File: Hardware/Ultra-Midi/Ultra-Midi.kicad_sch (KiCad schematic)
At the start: 28 parts, among them J1 Conn_01x02, J14 CUI_SD-50BV, J16 CUI_SD-50BV, J17 CUI_SD-50BV, J2 Conn_01x02, J3 Conn_01x02, J4 Conn_01x06, U1 ADuM226, U2 AP7370

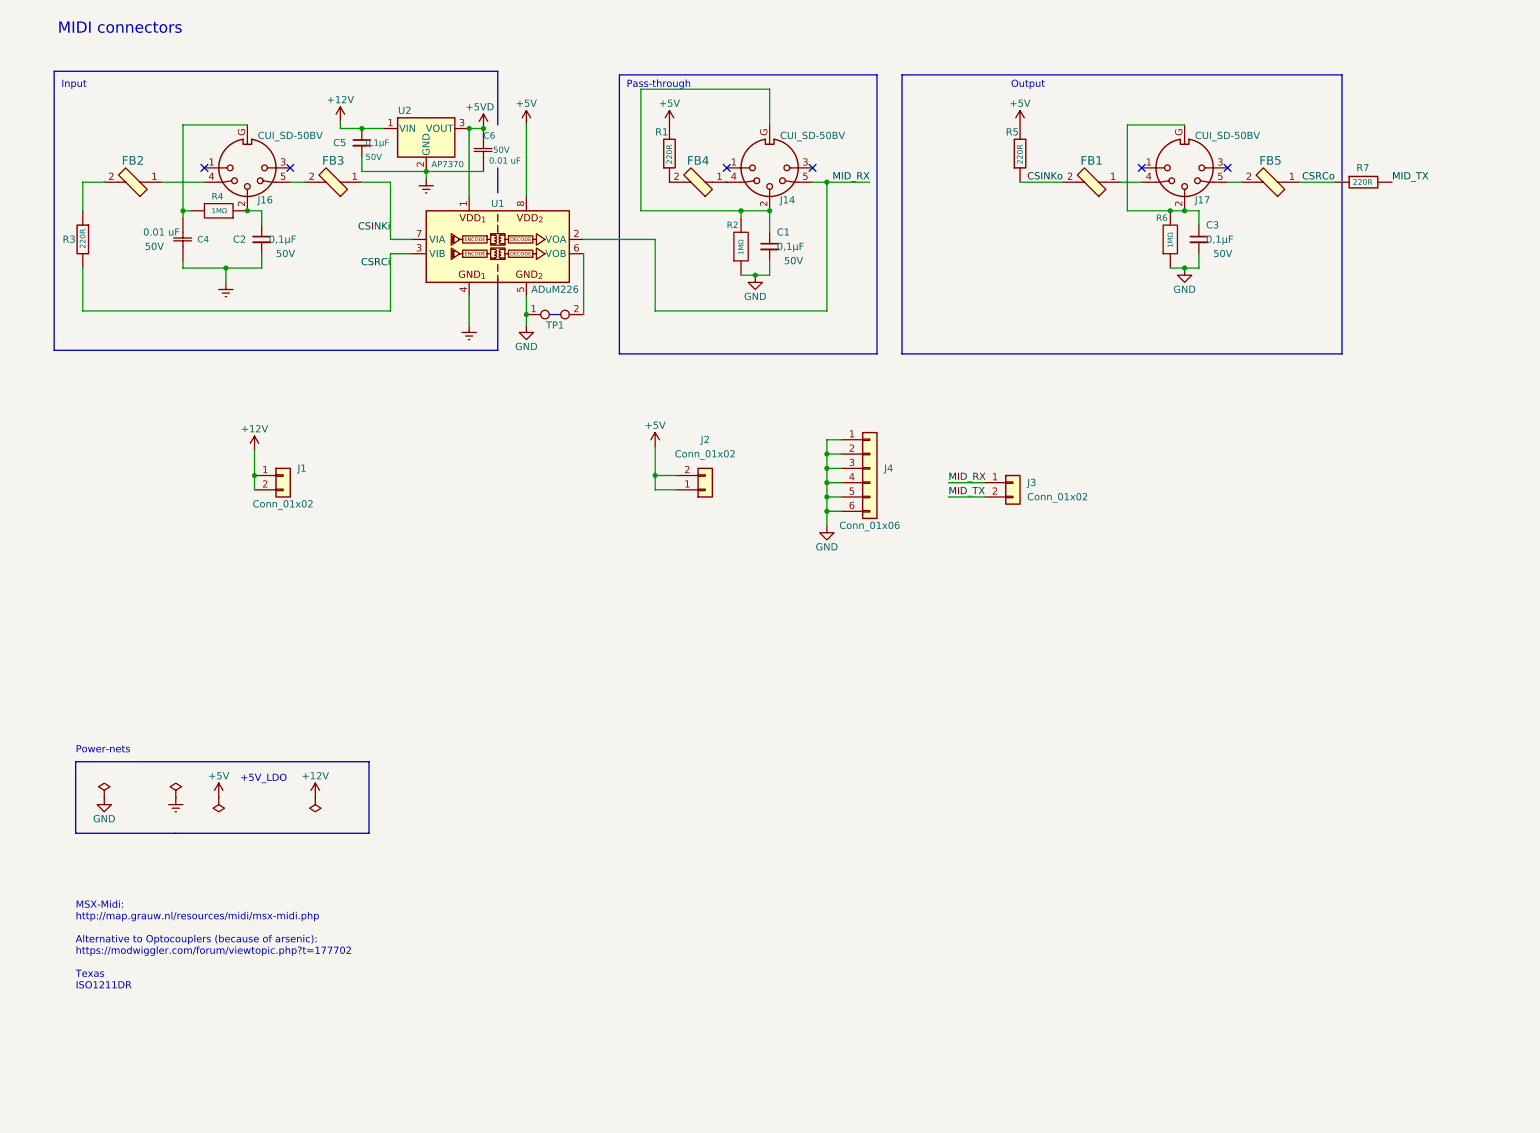
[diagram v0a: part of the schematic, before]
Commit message: Redesigned VDP-board to include a socket, increased it to 4 layers. Various clean-ups here and there. Improved the printer-port and joystick-port 3D-models. Improved the cooling-fin 3D-model, and added attachment-spring in 3D-model.
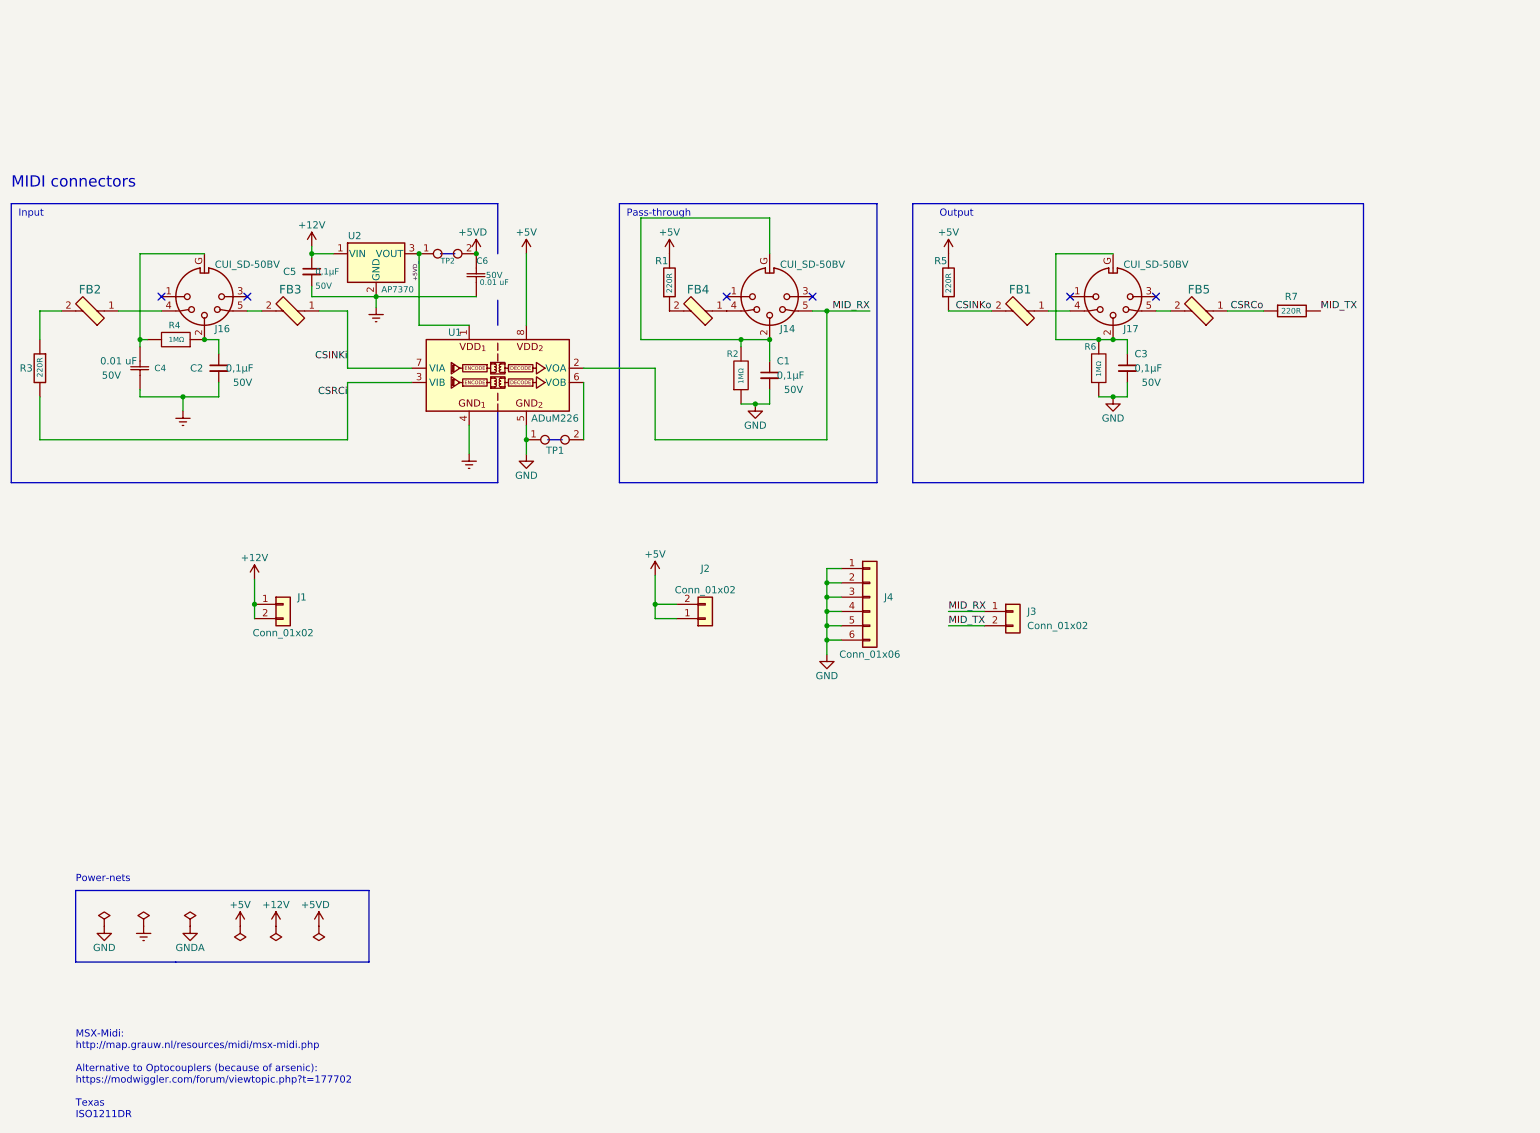
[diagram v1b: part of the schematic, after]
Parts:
- added TP2: TestPoint_2Pole, NetTie:NetTie-2_SMD_Pad0.5mm, symbol Connector:TestPoint_2Pole
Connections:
- net +5VD: now also TP2.2; no longer U1.1 (VDD1), U2.3 (VOUT)
- new net +5VD_: TP2.1, U1.1 (VDD1), U2.3 (VOUT)
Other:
- note removed: "+5V_LDO"
- moved on the sheet: C1, C2, C3, C4, C5, C6, FB1, FB2, FB3, FB4, FB5, J1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
